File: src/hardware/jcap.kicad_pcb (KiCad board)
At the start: 2 copper layers, 136.8 x 87 mm, 66 parts, among them J201 CPU PGMR, J202 SPARE CPU HDR, J203 GPU PGMR, J204 SPARE GPU HDR, J301 DC IN, J501 VGA OUT, J601 CONTROLS, Q301 IPP80P03P4L-04, SW201 CPU ~{RES}, SW202 DEBUG, SW203 GPU ~{RES}, SW601 TILT, U201 P8X32A, U202 P8X32A, U301 LM3940IT, U401 24LC256, U402 24LC256, U601 74HC165, U602 74HC165, Y201 6.5MHz, Y202 6.5MHz

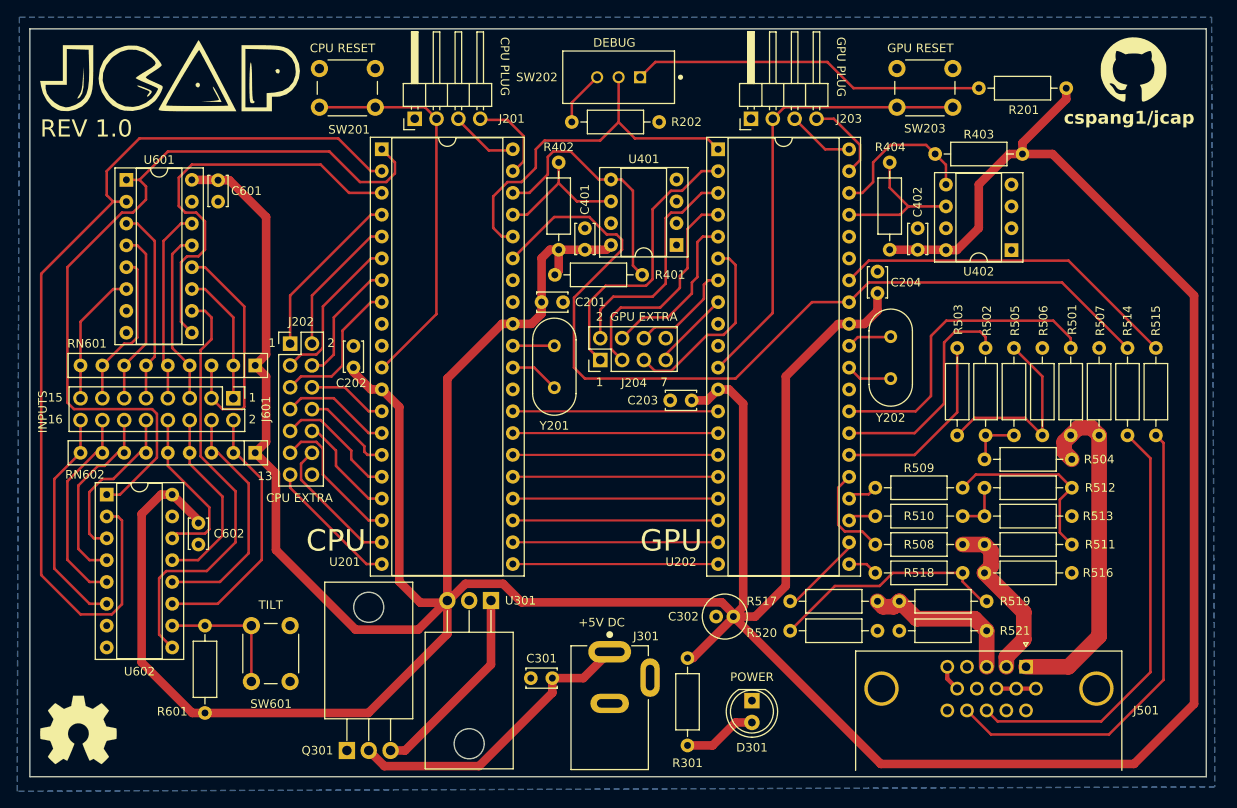
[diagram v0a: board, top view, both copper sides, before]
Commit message: Fixed sync pin mixup - Rev 2.0
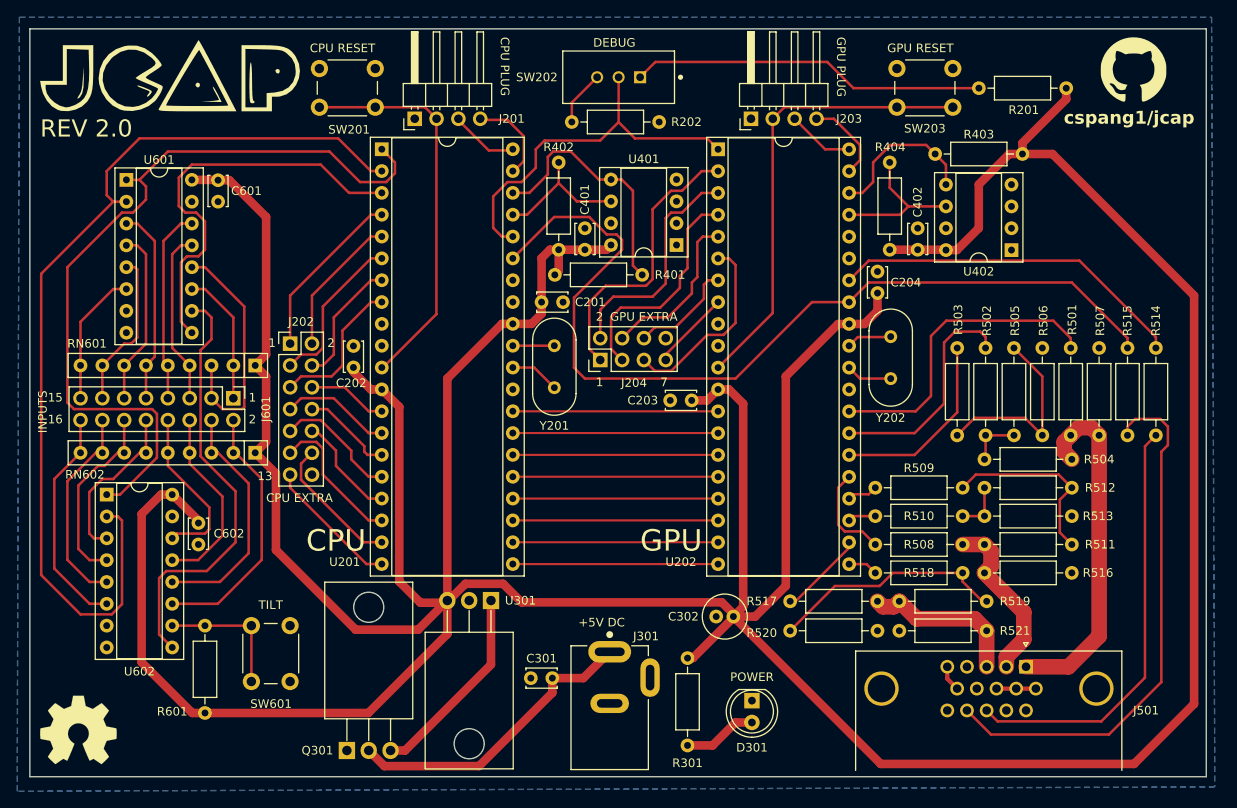
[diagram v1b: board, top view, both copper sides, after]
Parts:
- R507, R516: value 146 -> 147
- R517, R518, R520: value 266 -> 267
- R521: value 173 -> 174
- moved R514 3.30 mm to (208.7, 88.5)
- moved R515 3.30 mm to (205.4, 88.5)
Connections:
- R514 pad 1: V_SYNC -> H_SYNC
- R515 pad 1: H_SYNC -> V_SYNC
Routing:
- net Net-(J501-Pad14): track 55.5 -> 62.8 mm
- net Net-(J501-Pad13): track 50.6 -> 49.8 mm
- net H_SYNC: track 40.8 -> 41.6 mm
- net V_SYNC: track 105.7 -> 106.3 mm
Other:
- board text added: "REV 2.0"
- board text removed: "REV 1.0"
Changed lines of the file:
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@@
         (effects (font (size 1 1) (thickness 0.15)))
     )
-    (fp_text value "146" (at -2.794 0.035275 90) (layer "F.Fab")
+    (fp_text value "147" (at -2.794 0.035275 90) (layer "F.Fab")
         (effects (font (size 1 1) (thickness 0.15)))
     )
@@
         (effects (font (size 1 1) (thickness 0.15)))
     )
-    (fp_text value "266" (at 5.08 2.37) (layer "F.Fab")
+    (fp_text value "267" (at 5.08 2.37) (layer "F.Fab")
         (effects (font (size 1 1) (thickness 0.15)))
     )
@@
   )
   (footprint "Resistor_THT:R_Axial_DIN0207_L6.3mm_D2.5mm_P10.16mm_Horizontal" (layer "F.Cu")
-    (at 208.661 88.519 -90)
+    (at 205.359 88.519 -90)
     (descr "Resistor, Axial_DIN0207 series, Axial, Horizontal, pin pitch=10.16mm, 0.25W = 1/4W, length*diameter=6.3*2.5mm^2, http://cdn-reichelt.de/documents/datenblatt/B400/1_4W%23YAG.pdf")
     (tags "Resistor Axial_DIN0207 series Axial Horizontal pin pitch 10.16mm 0.25W = 1/4W length 6.3mm diameter 2.5mm")
@@
       (stroke (width 0.1) (type solid)) (layer "F.Fab"))
     (pad "1" thru_hole circle (at 0 0 270) (size 1.6 1.6) (drill 0.8) (layers "*.Cu" "*.Mask")
-      (net 43 "H_SYNC") (pintype "passive"))
+      (net 44 "V_SYNC") (pintype "passive"))
     (pad "2" thru_hole oval (at 10.16 0 270) (size 1.6 1.6) (drill 0.8) (layers "*.Cu" "*.Mask")
       (net 90 "Net-(J501-Pad14)") (pintype "passive"))
@@
         (effects (font (size 1 1) (thickness 0.15)))
     )
-    (fp_text value "266" (at 5.08 2.37) (layer "F.Fab")
+    (fp_text value "267" (at 5.08 2.37) (layer "F.Fab")
         (effects (font (size 1 1) (thickness 0.15)))
     )
@@
         (effects (font (size 1 1) (thickness 0.15)))
     )
-    (fp_text value "173" (at 5.08 2.37) (layer "F.Fab")
+    (fp_text value "174" (at 5.08 2.37) (layer "F.Fab")
         (effects (font (size 1 1) (thickness 0.15)))
     )
@@
         (effects (font (size 1 1) (thickness 0.15)))
     )
-    (fp_text value "146" (at 12.954 -0.07055) (layer "F.Fab")
+    (fp_text value "147" (at 12.954 -0.07055) (layer "F.Fab")
         (effects (font (size 1 1) (thickness 0.15)))
     )
@@
   )
   (footprint "Resistor_THT:R_Axial_DIN0207_L6.3mm_D2.5mm_P10.16mm_Horizontal" (layer "F.Cu")
-    (at 205.359 88.519 -90)
+    (at 208.661 88.519 -90)
     (descr "Resistor, Axial_DIN0207 series, Axial, Horizontal, pin pitch=10.16mm, 0.25W = 1/4W, length*diameter=6.3*2.5mm^2, http://cdn-reichelt.de/documents/datenblatt/B400/1_4W%23YAG.pdf")
     (tags "Resistor Axial_DIN0207 series Axial Horizontal pin pitch 10.16mm 0.25W = 1/4W length 6.3mm diameter 2.5mm")
@@
       (stroke (width 0.1) (type solid)) (layer "F.Fab"))
     (pad "1" thru_hole circle (at 0 0 270) (size 1.6 1.6) (drill 0.8) (layers "*.Cu" "*.Mask")
-      (net 44 "V_SYNC") (pintype "passive"))
+      (net 43 "H_SYNC") (pintype "passive"))
     (pad "2" thru_hole oval (at 10.16 0 270) (size 1.6 1.6) (drill 0.8) (layers "*.Cu" "*.Mask")
       (net 89 "Net-(J501-Pad13)") (pintype "passive"))
@@
         (effects (font (size 1 1) (thickness 0.15)))
     )
-    (fp_text value "266" (at 5.08 2.37) (layer "F.Fab")
+    (fp_text value "267" (at 5.08 2.37) (layer "F.Fab")
         (effects (font (size 1 1) (thickness 0.15)))
     )
@@
     (effects (font (size 1 1) (thickness 0.15)) (justify bottom))
   )
-  (gr_text "REV 1.0" (at 78.866879 64.165073) (layer "F.SilkS")
+  (gr_text "REV 2.0" (at 78.866879 64.165073) (layer "F.SilkS")
     (effects (font (size 2 2) (thickness 0.3)) (justify left bottom))
   )
@@
   (segment (start 172.974 113.665) (end 175.006 113.665) (width 0.3) (layer "F.Cu") (net 42))
   (segment (start 175.006 113.665) (end 176.022 114.681) (width 0.3) (layer "F.Cu") (net 42))
-  (segment (start 198.501 78.359) (end 175.26 78.359) (width 0.3) (layer "F.Cu") (net 43))
-  (segment (start 208.661 88.519) (end 198.501 78.359) (width 0.3) (layer "F.Cu") (net 43))
   (segment (start 175.26 78.359) (end 172.974 80.645) (width 0.3) (layer "F.Cu") (net 43))
+  (segment (start 208.661 87.249) (end 199.771 78.359) (width 0.3) (layer "F.Cu") (net 43))
+  (segment (start 199.771 78.359) (end 175.26 78.359) (width 0.3) (layer "F.Cu") (net 43))
+  (segment (start 208.661 88.519) (end 208.661 87.249) (width 0.3) (layer "F.Cu") (net 43))
   (segment (start 140.97 90.805) (end 142.24 92.075) (width 0.3) (layer "F.Cu") (net 44))
-  (segment (start 197.739 80.899) (end 175.26 80.899) (width 0.3) (layer "F.Cu") (net 44))
   (segment (start 142.24 92.075) (end 159.766 92.075) (width 0.3) (layer "F.Cu") (net 44))
   (segment (start 133.853 78.095) (end 138.669 73.279) (width 0.3) (layer "F.Cu") (net 44))
-  (segment (start 205.359 88.519) (end 197.739 80.899) (width 0.3) (layer "F.Cu") (net 44))
+  (segment (start 198.882 80.899) (end 175.26 80.899) (width 0.3) (layer "F.Cu") (net 44))
   (segment (start 138.669 73.279) (end 142.748 73.279) (width 0.3) (layer "F.Cu") (net 44))
+  (segment (start 205.359 87.376) (end 198.882 80.899) (width 0.3) (layer "F.Cu") (net 44))
   (segment (start 146.558 77.089) (end 140.97 82.677) (width 0.3) (layer "F.Cu") (net 44))
   (segment (start 159.766 92.075) (end 168.656 83.185) (width 0.3) (layer "F.Cu") (net 44))
   (segment (start 142.748 73.279) (end 144.78 75.311) (width 0.3) (layer "F.Cu") (net 44))
-  (segment (start 175.26 80.899) (end 172.974 83.185) (width 0.3) (layer "F.Cu") (net 44))
+  (segment (start 205.359 88.519) (end 205.359 87.376) (width 0.3) (layer "F.Cu") (net 44))
   (segment (start 144.78 75.311) (end 145.923 75.311) (width 0.3) (layer "F.Cu") (net 44))
+  (segment (start 175.26 80.899) (end 172.974 83.185) (width 0.3) (layer "F.Cu") (net 44))
   (segment (start 146.558 75.946) (end 146.558 77.089) (width 0.3) (layer "F.Cu") (net 44))
   (segment (start 145.923 75.311) (end 146.558 75.946) (width 0.3) (layer "F.Cu") (net 44))
@@
   (segment (start 148.6635 57.023) (end 150.4415 55.245) (width 0.3) (layer "F.Cu") (net 82))
   (segment (start 170.434 55.245) (end 173.482 58.293) (width 0.3) (layer "F.Cu") (net 82))
+  (segment (start 207.391 126.873) (end 202.311 131.953) (width 0.3) (layer "F.Cu") (net 89))
   (segment (start 190.246 131.953) (end 188.976 130.683) (width 0.3) (layer "F.Cu") (net 89))
-  (segment (start 205.359 98.679) (end 208.026 101.346) (width 0.3) (layer "F.Cu") (net 89))
+  (segment (start 208.661 98.679) (end 207.391 99.949) (width 0.3) (layer "F.Cu") (net 89))
+  (segment (start 207.391 99.949) (end 207.391 126.873) (width 0.3) (layer "F.Cu") (net 89))
   (segment (start 202.311 131.953) (end 190.246 131.953) (width 0.3) (layer "F.Cu") (net 89))
-  (segment (start 208.026 126.238) (end 202.311 131.953) (width 0.3) (layer "F.Cu") (net 89))
-  (segment (start 208.026 101.346) (end 208.026 126.238) (width 0.3) (layer "F.Cu") (net 89))
-  (segment (start 209.55 99.568) (end 209.55 127.127) (width 0.3) (layer "F.Cu") (net 90))
-  (segment (start 209.55 127.127) (end 203.2 133.477) (width 0.3) (layer "F.Cu") (net 90))
   (segment (start 189.48 133.477) (end 186.686 130.683) (width 0.3) (layer "F.Cu") (net 90))
+  (segment (start 210.058 97.663) (end 210.058 99.822) (width 0.3) (layer "F.Cu") (net 90))
+  (segment (start 209.169 96.774) (end 210.058 97.663) (width 0.3) (layer "F.Cu") (net 90))
+  (segment (start 205.359 97.663) (end 206.248 96.774) (width 0.3) (layer "F.Cu") (net 90))
+  (segment (start 205.359 98.679) (end 205.359 97.663) (width 0.3) (layer "F.Cu") (net 90))
+  (segment (start 209.296 127.381) (end 203.2 133.477) (width 0.3) (layer "F.Cu") (net 90))
   (segment (start 203.2 133.477) (end 189.48 133.477) (width 0.3) (layer "F.Cu") (net 90))
-  (segment (start 208.661 98.679) (end 209.55 99.568) (width 0.3) (layer "F.Cu") (net 90))
+  (segment (start 210.058 99.822) (end 209.296 100.584) (width 0.3) (layer "F.Cu") (net 90))
+  (segment (start 209.296 100.584) (end 209.296 127.381) (width 0.3) (layer "F.Cu") (net 90))
+  (segment (start 206.248 96.774) (end 209.169 96.774) (width 0.3) (layer "F.Cu") (net 90))
   (segment (start 188.849 98.679) (end 188.849 101.346) (width 0.3) (layer "F.Cu") (net 92))
   (segment (start 188.849 98.679) (end 192.151 98.679) (width 0.3) (layer "F.Cu") (net 92))

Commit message: Added silkscreen idents & fixed missing gnd pin on input hdr
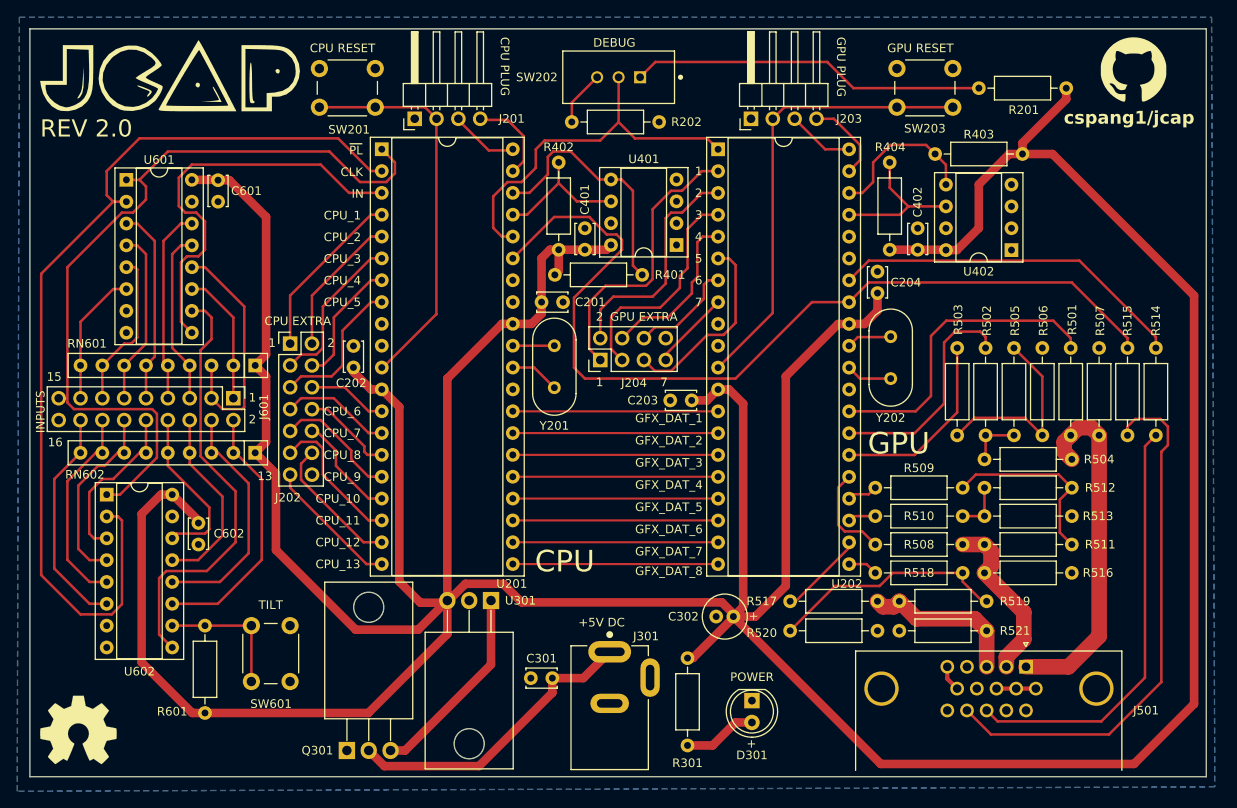
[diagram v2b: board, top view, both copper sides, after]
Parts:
- J601: footprint Connector_PinHeader_2.54mm:PinHeader_2x08_P2.54mm_Vertical -> Connector_PinHeader_2.54mm:PinHeader_2x09_P2.54mm_Vertical
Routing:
- net /Propellers/GPU_SPARE_7: track 8.61 -> 9.25 mm
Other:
- board text added: "+"
- board text added: "3"
- board text added: "4"
- board text added: "5"
- board text added: "6"
- board text added: "CLK"
- board text added: "CPU_1"
- board text added: "CPU_10"
- board text added: "CPU_11"
- board text added: "CPU_12"
- board text added: "CPU_13"
- board text added: "CPU_2"
- board text added: "CPU_3"
- board text added: "CPU_4"
- board text added: "CPU_5"
- board text added: "CPU_6"
- board text added: "CPU_7"
- board text added: "CPU_8"
- board text added: "CPU_9"
- board text added: "GFX_DAT_1"
- board text added: "GFX_DAT_2"
- board text added: "GFX_DAT_3"
- board text added: "GFX_DAT_4"
- board text added: "GFX_DAT_5"
- board text added: "GFX_DAT_6"
- board text added: "GFX_DAT_7"
- board text added: "GFX_DAT_8"
- board text added: "IN"
- board text added: "~{PL}"
